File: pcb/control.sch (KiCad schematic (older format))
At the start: 35 parts

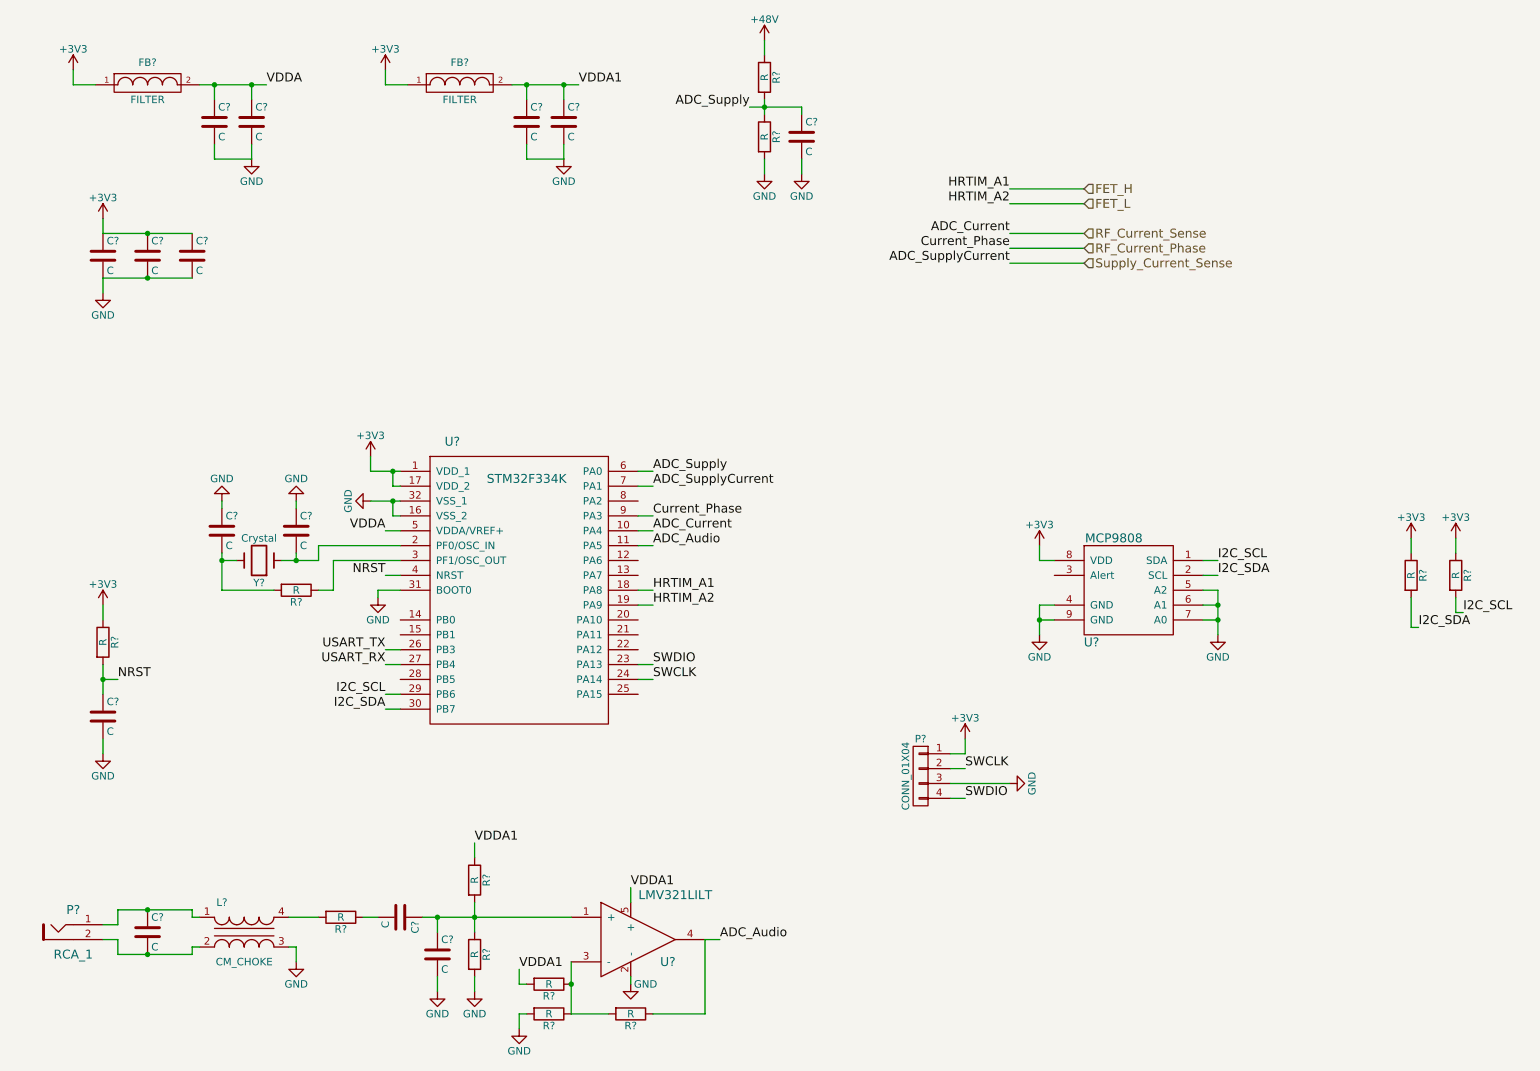
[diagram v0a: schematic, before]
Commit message: new GaN test board
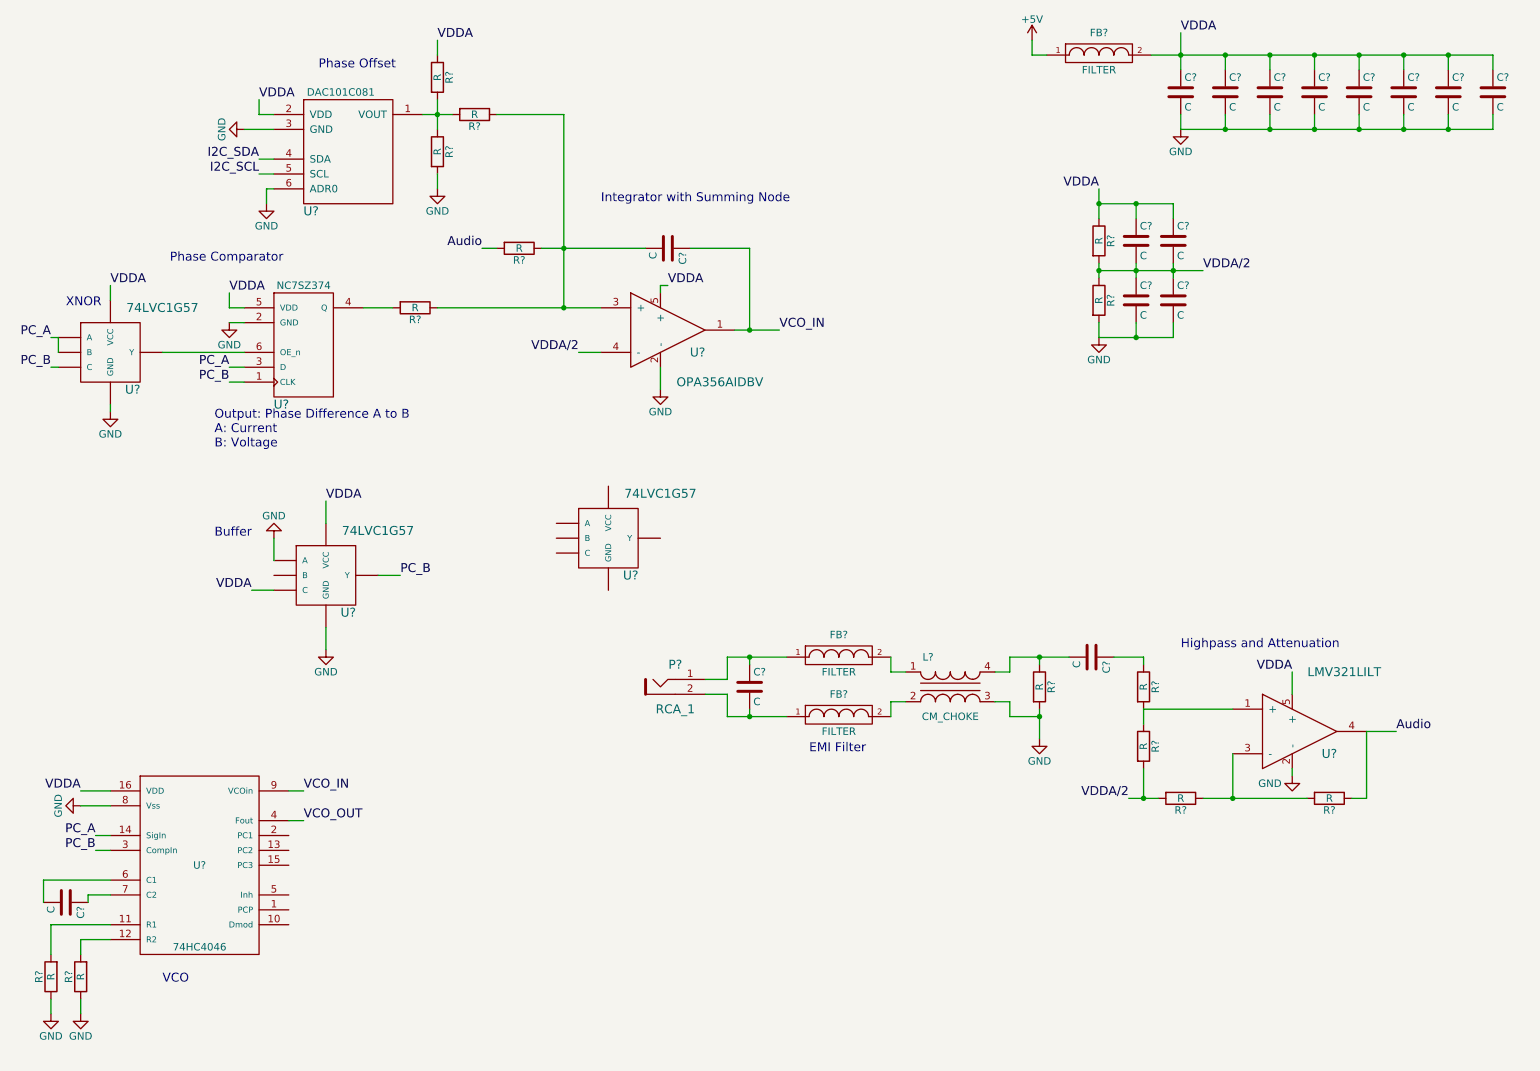
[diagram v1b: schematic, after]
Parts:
- removed C? (x14): C, symbol C
- removed FB? (x2): FILTER, symbol FILTER
- removed L?: CM_CHOKE, symbol CM_CHOKE
- removed P?: RCA_1, symbol RCA_1
- removed P?: CONN_01X04, symbol CONN_01X04
- removed R? (x12): R, symbol R
- removed U?: STM32F334K, symbol STM32F334K
- removed U?: MCP9808, symbol MCP9808
- removed U?: LMV321LILT, symbol LMV321LILT
- removed Y?: Crystal, symbol Crystal
- added C? (x16): C, symbol C
- added FB? (x3): FILTER, symbol FILTER
- added L?: CM_CHOKE, symbol CM_CHOKE
- added P?: RCA_1, symbol RCA_1
- added R? (x14): R, symbol R
- added U?: 74HC4046, symbol 74HC4046
- added U?: NC7SZ374, symbol NC7SZ374
- added U? (x3): 74LVC1G57, symbol 74LVC1G57
- added U?: OPA356AIDBV, symbol OPA356AIDBV
- added U?: DAC101C081, symbol DAC101C081
- added U?: LMV321LILT, symbol LMV321LILT
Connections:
- net GND: now also C?.2, C?.2, C?.2, C?.2, C?.2, C?.2, C?.2, C?.2, C?.2, C?.2, L?.3, R?.1, R?.1, R?.2, R?.2, R?.2, U?.2 (-), U?.2 (-), U?.2 (GND), U?.2 (GND), U?.2 (GND), U?.3 (A), U?.3 (GND), U?.6 (ADR0), U?.8 (Vss)
- net I2C_SCL: now also U?.5 (SCL)
- net I2C_SDA: now also U?.4 (SDA)
- net VDDA: now also C?.1, C?.1, C?.1, C?.1, C?.1, C?.1, C?.1, C?.1, C?.1, C?.1, FB?.2, R?.1, R?.1, U?.16 (VDD), U?.2 (VDD), U?.5 (+), U?.5 (+), U?.5 (VCC), U?.5 (VCC), U?.5 (VDD), U?.6 (C)
- new net: R?.2, U?.11 (R1)
- new net: R?.2, U?.12 (R2)
- new net: C?.2, U?.6 (C1)
- new net: C?.1, U?.7 (C2)
- new net: R?.2, U?.4 (Q)
- new net: U?.4 (Y), U?.6 (OE_n)
- new net: C?.2, R?.1, R?.1, R?.1, U?.3 (+)
- new net: R?.1, R?.2, R?.2, U?.1 (VOUT)
- new net: R?.1, R?.2, U?.1 (+)
- new net: R?.1, R?.2, U?.3 (-)
- new net: C?.1, FB?.1, P?.1
- new net: C?.2, FB?.1, P?.2
- new net: FB?.2, L?.1
- new net: FB?.2, L?.2
- new net: C?.2, L?.4, R?.1
- new net: C?.1, R?.1
- new net +5V: FB?.1
- new net Audio: R?.1, R?.2, U?.4
- new net PC_A: U?.1 (B), U?.14 (SigIn), U?.3 (A), U?.3 (D)
- new net PC_B: U?.1 (CLK), U?.3 (CompIn), U?.4 (Y), U?.6 (C)
- new net VCO_IN: C?.1, U?.1, U?.9 (VCOin)
- new net VCO_OUT: U?.4 (Fout)
- new net VDDA/2: C?.1, C?.1, C?.2, C?.2, R?.1, R?.2, R?.2, R?.2, U?.4 (-)
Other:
- note added: "Buffer"
- note added: "EMI Filter"
- note added: "Highpass and Attenuation"
- note added: "Integrator with Summing Node"
- note added: "Output: Phase Difference A to B\nA: Current\nB: Voltage"
- note added: "Phase Comparator"
- note added: "Phase Offset"
- note added: "VCO"
- note added: "XNOR"
